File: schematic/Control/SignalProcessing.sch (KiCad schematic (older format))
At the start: 16 parts

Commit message: Control board diagram complete at high level - Clock, USB, Control, Power and IO done. Remaining is FPGA pin assignment which will be done later to optimize board layout.
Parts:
- removed U?: TPS79333-EP, Package_TO_SOT_SMD:SOT-23-5, symbol Regulator_Linear:TPS79333-EP
- added C? (x10): 100nF, Capacitor_SMD:C_0603_1608Metric, symbol Device:C
- added C? (x4): 10uF, Capacitor_SMD:C_0603_1608Metric, symbol Device:C
- added C? (x3): 10nF, Capacitor_SMD:C_0603_1608Metric, symbol Device:C
- added L? (x2): 100 Ohm@100MHz, Inductor_SMD:L_0805_2012Metric, symbol Device:L_Core_Ferrite
- added R?: 10k/DNP, Resistor_SMD:R_0603_1608Metric, symbol Device:R
- added R?: 10k, Resistor_SMD:R_0603_1608Metric, symbol Device:R
- added U?: TPS79333-EP, Package_TO_SOT_SMD:SOT-23-5, symbol Regulator_Linear:TPS79333-EP
- added U?: TPS73633DCQ, Package_TO_SOT_SMD:SOT-223-6_TabPin3, symbol Zmei_elements:TPS73601DCQ
- U?: value TPS73618DBVR -> TLV74112PDBVR
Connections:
- net labels added: +1V2_FPGA, +3V3_FPGA, +3V3_IO, +5V, I2S1_BCK_IN, I2S1_DATA_IN, I2S1_LRCK_IN, I2S2_BCK_IN, I2S2_DATA_IN, I2S_BCKL_OUT, I2S_BCKR_OUT, I2S_DATAL_OUT, I2S_DATAR_OUT, I2S_LRCKL_OUT, I2S_LRCKR_OUT, I2S_LRCK_IN, SPDIF1_IN, SPDIF2_IN, TCK, TDI, TDO, TMS, ~RST~
- net labels removed: +3V3_CLKOUT, BCK_OUT, DATA_OUT, LRCK_OUT
- wire segments 123 -> 204
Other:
- moved on the sheet: C?, U?, U?C, U?E, U?F

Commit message: Provision for SPI Slave FPGA bitstream download. Switch RAM from x16 to x8 one.
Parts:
- removed U?: IS61WV25616E, Package_SO:TSOP-II-44_10.16x18.41mm_P0.8mm, symbol Zmei_elements:IS61WV25616E
- added C425, C426, C427, C428, C429, C430, C431, C432, C433, C434, C435, C436, C437, C438: 100nF, Capacitor_SMD:C_0603_1608Metric, symbol Device:C
- added JP401: SolderJumper_2_Open, Jumper:SolderJumper-2_P1.3mm_Open_RoundedPad1.0x1.5mm, symbol Jumper:SolderJumper_2_Open
- added R403, R404: 10k, Resistor_SMD:R_0603_1608Metric, symbol Device:R
- added RN401: RA1206 10k, Resistor_SMD:R_Array_Convex_4x0603, symbol Device:R_Pack04
- added U?: IS61WV5128FBLL, Package_SO:TSOP-II-44_10.16x18.41mm_P0.8mm, symbol Zmei_elements:IS61WV5128FBLL
- gave numbers to parts that had none: 32
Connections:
- net labels added: DONE, ~INIT~, ~PROGRAM~
- net labels removed: A0, A1, A10, A11, A12, A13, A14, A15, A16, A17, A18, A2, A3, A4, A5, A6, A7, A8, A9, D0, D1, D10, D11, D12, D13, D14, D15, D2, D3, D4, D5, D6, D7, D8, D9, ~RAM_CS~, ~RAM_LB~, ~RAM_OE~, ~RAM_UB~, ~RAM_WE~, ~RST~
- wire segments 204 -> 209
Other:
- moved on the sheet: U401A, U401B, U401C, U401D

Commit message: Interim commit
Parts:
- removed JP401: SolderJumper_2_Open, Jumper:SolderJumper-2_P1.3mm_Open_RoundedPad1.0x1.5mm, symbol Jumper:SolderJumper_2_Open
- removed RN401: RA1206 10k, Resistor_SMD:R_Array_Convex_4x0603, symbol Device:R_Pack04
- added C?: 220uF/10V, Capacitor_SMD:C_Elec_8x6.2, symbol Device:CP
- added R405, R406, R407, R408, R409: 10k, Resistor_SMD:R_0603_1608Metric, symbol Device:R
- added TP401: TestPoint, TestPoint:TestPoint_Pad_D1.0mm, symbol Connector:TestPoint
- gave numbers to parts that had none: 1
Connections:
- net labels added: A0, A1, A10, A11, A12, A13, A14, A15, A16, A17, A18, A19, A2, A20, A3, A4, A5, A6, A7, A8, A9, FPGA_LED, I2S1_SCK_IN, I2S2_LRCK_IN, I2S2_SCK_IN, IO0, IO1, IO2, IO3, IO4, IO5, IO6, IO7, ~OE~, ~RST~, ~WE~
- net labels removed: I2S_LRCK_IN
- wire segments 209 -> 287
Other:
- moved on the sheet: R403, R404

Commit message: Routing complete
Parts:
- removed C413, C419: 10nF, Capacitor_SMD:C_0603_1608Metric, symbol Device:C
- removed C415, C422: 10uF, Capacitor_SMD:C_0603_1608Metric, symbol Device:C
- removed U404: TPS79333-EP, Package_TO_SOT_SMD:SOT-23-5, symbol Regulator_Linear:TPS79333-EP
- added C413: 47uF/6.3V, Capacitor_Tantalum_SMD:CP_EIA-3528-12_Kemet-T, symbol Device:CP
- added C440: 100uF/10V, Capacitor_SMD:C_Elec_6.3x5.4, symbol Device:CP
- added J401: JTAG, Connector_PinHeader_2.54mm:PinHeader_1x06_P2.54mm_Vertical, symbol Connector_Generic:Conn_01x06
- C424: value 220uF/10V -> 100uF/10V; footprint Capacitor_SMD:C_Elec_8x6.2 -> Capacitor_SMD:C_Elec_6.3x5.4
- C439: renamed from C?; value 220uF/10V -> 100uF/10V; footprint Capacitor_SMD:C_Elec_8x6.2 -> Capacitor_SMD:C_Elec_6.3x5.4
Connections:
- net labels added: ~FPGA_CS~
- wire segments 287 -> 286
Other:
- moved on the sheet: C416, C417, C420, C423, C424, L401, L402, R406, R407, R408, R409, U401F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

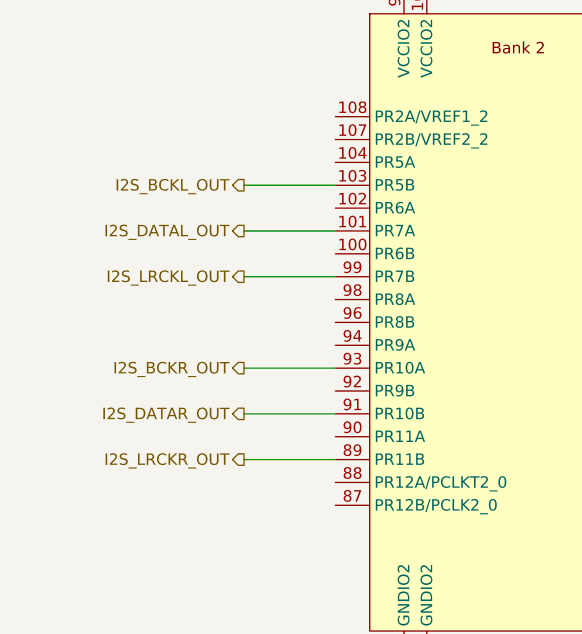
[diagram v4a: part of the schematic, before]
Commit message: Add source termination resistors to I2S output lines. Arrange top silk information.
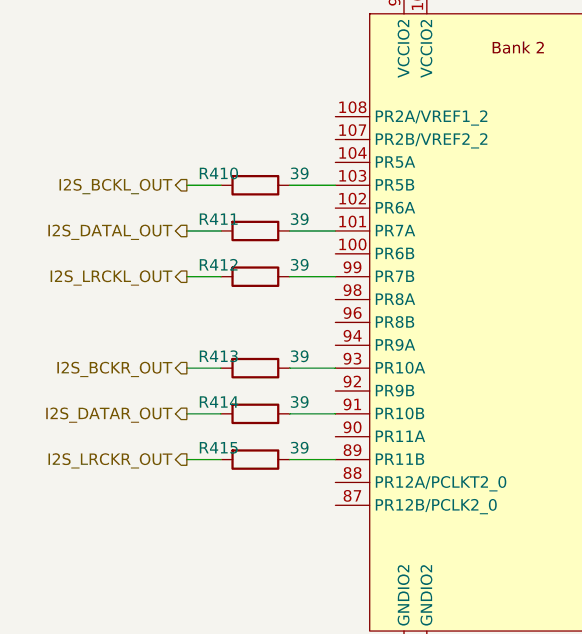
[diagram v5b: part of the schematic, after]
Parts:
- added R410, R411, R412, R413, R414, R415: 39, Resistor_SMD:R_0603_1608Metric, symbol Device:R
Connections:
- wire segments 286 -> 292
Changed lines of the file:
@@
 Text HLabel 14600 8200 2    50   Input ~ 0
 SCLK
-Text HLabel 1450 7800 0    50   Output ~ 0
+Text HLabel 1200 7800 0    50   Output ~ 0
 I2S_LRCKL_OUT
-Text HLabel 1450 7400 0    50   Output ~ 0
+Text HLabel 1200 7400 0    50   Output ~ 0
 I2S_BCKL_OUT
-Text HLabel 1450 7600 0    50   Output ~ 0
+Text HLabel 1200 7600 0    50   Output ~ 0
 I2S_DATAL_OUT
-Wire Wire Line
-	1450 7600 1850 7600
-Wire Wire Line
-	1850 7400 1450 7400
-Wire Wire Line
-	1450 7800 1850 7800
 Text HLabel 4400 2300 2    50   Input ~ 0
 SCK_IN
@@
 Wire Wire Line
 	14600 8500 13450 8500
-Text HLabel 1450 8400 0    50   Output ~ 0
+Text HLabel 1200 8400 0    50   Output ~ 0
 I2S_DATAR_OUT
-Wire Wire Line
-	1450 8400 1850 8400
-Text HLabel 1450 8600 0    50   Output ~ 0
+Text HLabel 1200 8600 0    50   Output ~ 0
 I2S_LRCKR_OUT
-Text HLabel 1450 8200 0    50   Output ~ 0
+Text HLabel 1200 8200 0    50   Output ~ 0
 I2S_BCKR_OUT
-Wire Wire Line
-	1850 8200 1450 8200
-Wire Wire Line
-	1450 8600 1850 8600
 Text HLabel 1500 3600 0    50   Input ~ 0
 I2S1_DATA_IN
@@
 Text Label 12200 2250 0    50   ~ 0
 +3V3_FPGA
+Wire Wire Line
+	1200 7400 1350 7400
+Wire Wire Line
+	1200 7600 1350 7600
+Wire Wire Line
+	1200 7800 1350 7800
+Wire Wire Line
+	1200 8200 1350 8200
+Wire Wire Line
+	1200 8400 1350 8400
+Wire Wire Line
+	1200 8600 1350 8600
+$Comp
+L Device:R R?
+U 1 1 5E7FFBA0
+P 1500 7400
+AR Path="/5DBF9B5A/5E7FFBA0" Ref="R?"  Part="1"
+AR Path="/5DCC3140/5E7FFBA0" Ref="R?"  Part="1"
+AR Path="/5DD2C0D9/5E7FFBA0" Ref="R?"  Part="1"
+AR Path="/5DDC09A7/5E7FFBA0" Ref="R?"  Part="1"
+AR Path="/5DCFEDFC/5E7FFBA0" Ref="R410"  Part="1"
+F 0 "R410" V 1450 7150 50  0000 L CNN
+F 1 "39" V 1450 7550 50  0000 L CNN
+F 2 "Resistor_SMD:R_0603_1608Metric" V 1430 7400 50  0001 C CNN
+F 3 "~" H 1500 7400 50  0001 C CNN
+	1    1500 7400
+	0    1    1    0
+$EndComp
+Wire Wire Line
+	1650 7400 1850 7400
+$Comp
+L Device:R R?
+U 1 1 5E8015F6
+P 1500 7600
+AR Path="/5DBF9B5A/5E8015F6" Ref="R?"  Part="1"
+AR Path="/5DCC3140/5E8015F6" Ref="R?"  Part="1"
+AR Path="/5DD2C0D9/5E8015F6" Ref="R?"  Part="1"
+AR Path="/5DDC09A7/5E8015F6" Ref="R?"  Part="1"
+AR Path="/5DCFEDFC/5E8015F6" Ref="R411"  Part="1"
+F 0 "R411" V 1450 7350 50  0000 L CNN
+F 1 "39" V 1450 7750 50  0000 L CNN
+F 2 "Resistor_SMD:R_0603_1608Metric" V 1430 7600 50  0001 C CNN
+F 3 "~" H 1500 7600 50  0001 C CNN
+	1    1500 7600
+	0    1    1    0
+$EndComp
+Wire Wire Line
+	1650 7600 1850 7600
+$Comp
+L Device:R R?
+U 1 1 5E801972
+P 1500 7800
+AR Path="/5DBF9B5A/5E801972" Ref="R?"  Part="1"
+AR Path="/5DCC3140/5E801972" Ref="R?"  Part="1"
+AR Path="/5DD2C0D9/5E801972" Ref="R?"  Part="1"
+AR Path="/5DDC09A7/5E801972" Ref="R?"  Part="1"
+AR Path="/5DCFEDFC/5E801972" Ref="R412"  Part="1"
+F 0 "R412" V 1450 7550 50  0000 L CNN
+F 1 "39" V 1450 7950 50  0000 L CNN
+F 2 "Resistor_SMD:R_0603_1608Metric" V 1430 7800 50  0001 C CNN
+F 3 "~" H 1500 7800 50  0001 C CNN
+	1    1500 7800
+	0    1    1    0
+$EndComp
+Wire Wire Line
+	1650 7800 1850 7800
+$Comp
+L Device:R R?
+U 1 1 5E801CEE
+P 1500 8200
+AR Path="/5DBF9B5A/5E801CEE" Ref="R?"  Part="1"
+AR Path="/5DCC3140/5E801CEE" Ref="R?"  Part="1"
+AR Path="/5DD2C0D9/5E801CEE" Ref="R?"  Part="1"
+AR Path="/5DDC09A7/5E801CEE" Ref="R?"  Part="1"
+AR Path="/5DCFEDFC/5E801CEE" Ref="R413"  Part="1"
+F 0 "R413" V 1450 7950 50  0000 L CNN
+F 1 "39" V 1450 8350 50  0000 L CNN
+F 2 "Resistor_SMD:R_0603_1608Metric" V 1430 8200 50  0001 C CNN
+F 3 "~" H 1500 8200 50  0001 C CNN
+	1    1500 8200
+	0    1    1    0
+$EndComp
+Wire Wire Line
+	1650 8200 1850 8200
+$Comp
+L Device:R R?
+U 1 1 5E80213C
+P 1500 8400
+AR Path="/5DBF9B5A/5E80213C" Ref="R?"  Part="1"
+AR Path="/5DCC3140/5E80213C" Ref="R?"  Part="1"
+AR Path="/5DD2C0D9/5E80213C" Ref="R?"  Part="1"
+AR Path="/5DDC09A7/5E80213C" Ref="R?"  Part="1"
+AR Path="/5DCFEDFC/5E80213C" Ref="R414"  Part="1"
+F 0 "R414" V 1450 8150 50  0000 L CNN
+F 1 "39" V 1450 8550 50  0000 L CNN
+F 2 "Resistor_SMD:R_0603_1608Metric" V 1430 8400 50  0001 C CNN
+F 3 "~" H 1500 8400 50  0001 C CNN
+	1    1500 8400
+	0    1    1    0
+$EndComp
+Wire Wire Line
+	1650 8400 1850 8400
+$Comp
+L Device:R R?
+U 1 1 5E80233E
+P 1500 8600
+AR Path="/5DBF9B5A/5E80233E" Ref="R?"  Part="1"
+AR Path="/5DCC3140/5E80233E" Ref="R?"  Part="1"
+AR Path="/5DD2C0D9/5E80233E" Ref="R?"  Part="1"
+AR Path="/5DDC09A7/5E80233E" Ref="R?"  Part="1"
+AR Path="/5DCFEDFC/5E80233E" Ref="R415"  Part="1"
+F 0 "R415" V 1450 8350 50  0000 L CNN
+F 1 "39" V 1450 8750 50  0000 L CNN
+F 2 "Resistor_SMD:R_0603_1608Metric" V 1430 8600 50  0001 C CNN
+F 3 "~" H 1500 8600 50  0001 C CNN
+	1    1500 8600
+	0    1    1    0
+$EndComp
+Wire Wire Line
+	1650 8600 1850 8600
 $EndSCHEMATC

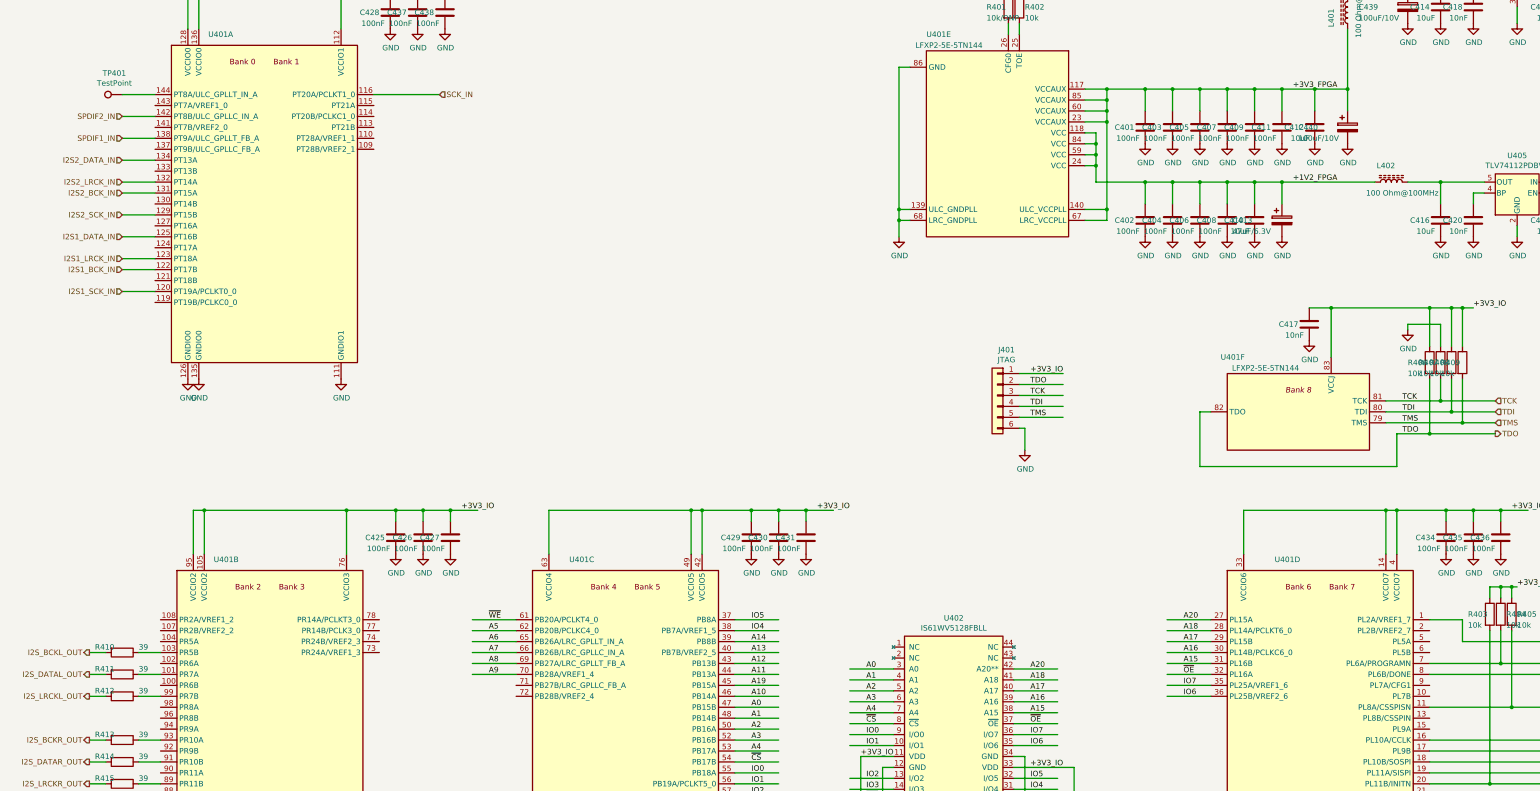
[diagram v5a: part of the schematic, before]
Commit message: Add some testpads. Fix +3V3_FPGA track mix-up after termination addition.
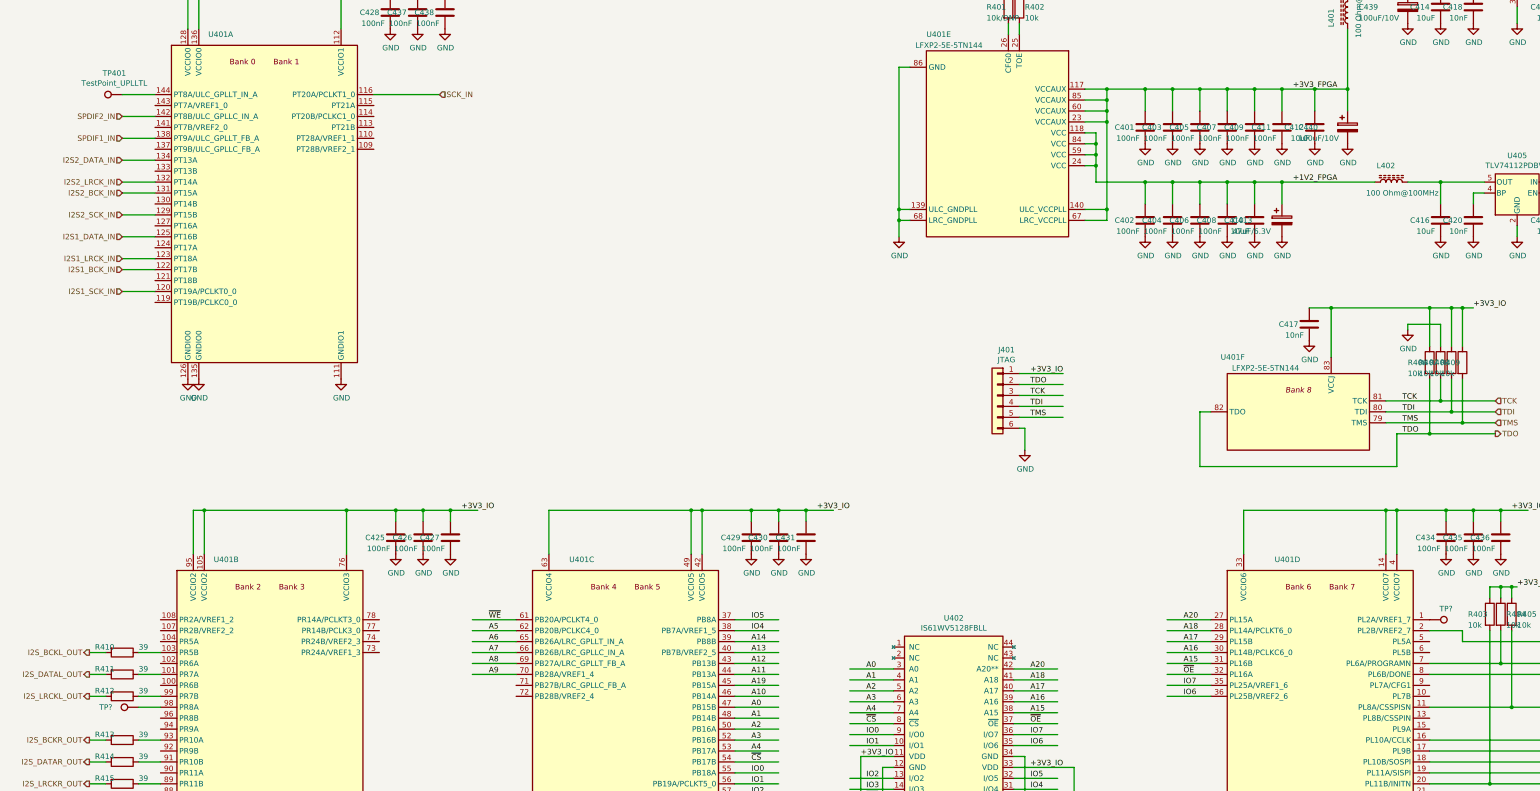
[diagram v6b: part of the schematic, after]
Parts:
- added TP?: TP_free1, TestPoint:TestPoint_Pad_D1.0mm, symbol Connector:TestPoint
- added TP?: TestPoint_free2, TestPoint:TestPoint_Pad_D1.0mm, symbol Connector:TestPoint
- TP401: value TestPoint -> TestPoint_UPLLTL
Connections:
- wire segments 292 -> 293
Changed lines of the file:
@@
 P 1500 2300
 F 0 "TP401" V 1695 2372 50  0000 C CNN
-F 1 "TestPoint" V 1604 2372 50  0000 C CNN
+F 1 "TestPoint_UPLLTL" V 1604 2372 50  0000 C CNN
 F 2 "TestPoint:TestPoint_Pad_D1.0mm" H 1700 2300 50  0001 C CNN
 F 3 "~" H 1700 2300 50  0001 C CNN
@@
 	14600 7300 13750 7300
 Wire Wire Line
-	13750 7300 13750 7100
-Wire Wire Line
-	13750 7100 13450 7100
+	13750 7300 13750 7200
+Wire Wire Line
+	13750 7200 13450 7200
 Text Label 14650 3100 0    50   ~ 0
 +3V3_IO
@@
 Wire Wire Line
 	1650 8600 1850 8600
+$Comp
+L Connector:TestPoint TP?
+U 1 1 5DE115AF
+P 13450 7100
+F 0 "TP?" V 13350 7250 50  0000 C CNN
+F 1 "TP_free1" V 13300 7150 50  0001 C CNN
+F 2 "TestPoint:TestPoint_Pad_D1.0mm" H 13650 7100 50  0001 C CNN
+F 3 "~" H 13650 7100 50  0001 C CNN
+	1    13450 7100
+	0    1    1    0
+$EndComp
+$Comp
+L Connector:TestPoint TP?
+U 1 1 5DE2E3D0
+P 1650 7900
+F 0 "TP?" V 1650 8200 50  0000 C CNN
+F 1 "TestPoint_free2" V 1550 8050 50  0001 C CNN
+F 2 "TestPoint:TestPoint_Pad_D1.0mm" H 1850 7900 50  0001 C CNN
+F 3 "~" H 1850 7900 50  0001 C CNN
+	1    1650 7900
+	0    -1   -1   0
+$EndComp
+Wire Wire Line
+	1850 7900 1650 7900
 $EndSCHEMATC

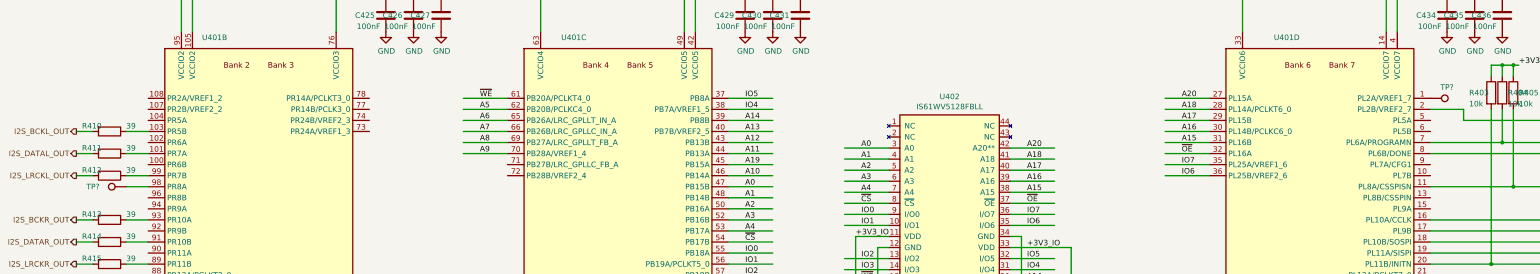
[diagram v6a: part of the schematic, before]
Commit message: Add decoupling cap between +5V and GND
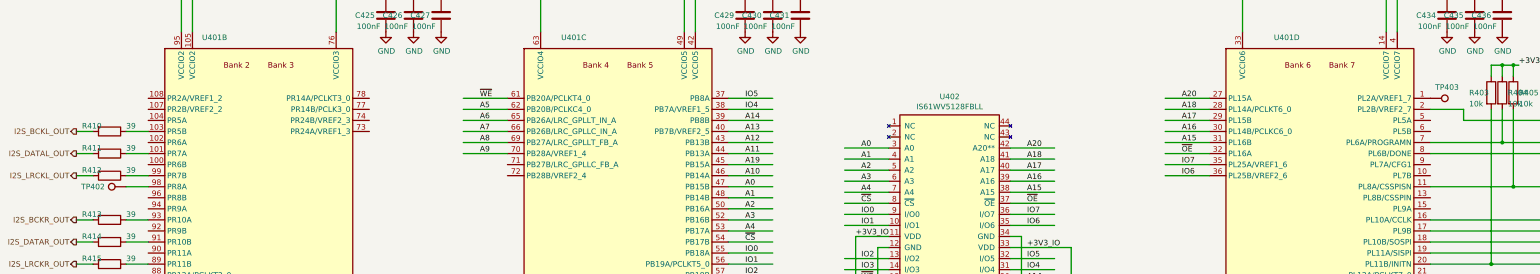
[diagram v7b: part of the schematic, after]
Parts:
- gave numbers to parts that had none: 2
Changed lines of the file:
@@
 	1650 8600 1850 8600
 $Comp
-L Connector:TestPoint TP?
+L Connector:TestPoint TP403
 U 1 1 5DE115AF
 P 13450 7100
-F 0 "TP?" V 13350 7250 50  0000 C CNN
+F 0 "TP403" V 13350 7250 50  0000 C CNN
 F 1 "TP_free1" V 13300 7150 50  0001 C CNN
 F 2 "TestPoint:TestPoint_Pad_D1.0mm" H 13650 7100 50  0001 C CNN
@@
 $EndComp
 $Comp
-L Connector:TestPoint TP?
+L Connector:TestPoint TP402
 U 1 1 5DE2E3D0
 P 1650 7900
-F 0 "TP?" V 1650 8200 50  0000 C CNN
+F 0 "TP402" V 1650 8200 50  0000 C CNN
 F 1 "TestPoint_free2" V 1550 8050 50  0001 C CNN
 F 2 "TestPoint:TestPoint_Pad_D1.0mm" H 1850 7900 50  0001 C CNN

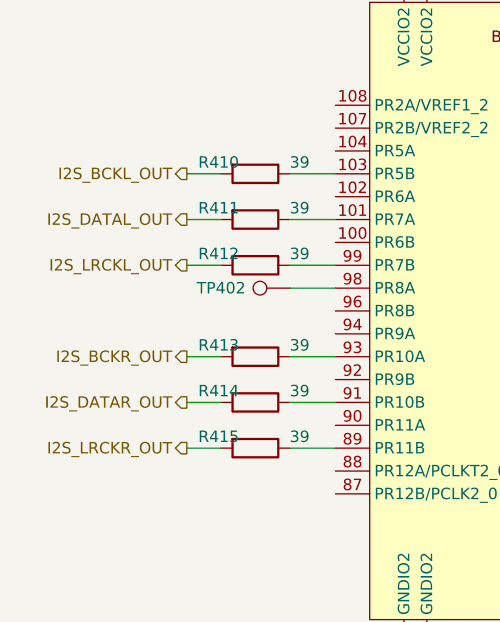
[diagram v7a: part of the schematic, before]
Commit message: Swap BCK and LRCK outputs. Misc small touch-ups on the board
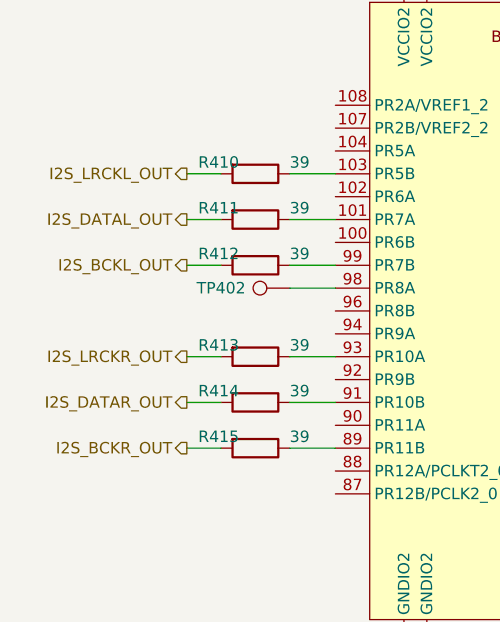
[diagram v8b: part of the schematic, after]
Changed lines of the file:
@@
 Text HLabel 14600 8200 2    50   Input ~ 0
 SCLK
+Text HLabel 1200 7400 0    50   Output ~ 0
+I2S_LRCKL_OUT
 Text HLabel 1200 7800 0    50   Output ~ 0
-I2S_LRCKL_OUT
-Text HLabel 1200 7400 0    50   Output ~ 0
 I2S_BCKL_OUT
 Text HLabel 1200 7600 0    50   Output ~ 0
@@
 Text HLabel 1200 8400 0    50   Output ~ 0
 I2S_DATAR_OUT
+Text HLabel 1200 8200 0    50   Output ~ 0
+I2S_LRCKR_OUT
 Text HLabel 1200 8600 0    50   Output ~ 0
-I2S_LRCKR_OUT
-Text HLabel 1200 8200 0    50   Output ~ 0
 I2S_BCKR_OUT
 Text HLabel 1500 3600 0    50   Input ~ 0
